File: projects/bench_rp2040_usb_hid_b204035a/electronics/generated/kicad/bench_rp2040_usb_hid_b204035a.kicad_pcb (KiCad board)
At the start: 2 copper layers, 51 x 21 mm, 14 parts, among them J1 USB-C POWER, J2 SWD 10-pin, U1 3V3 LDO, U2 RP2040, U3 2MB QSPI, X1 12MHz XTAL

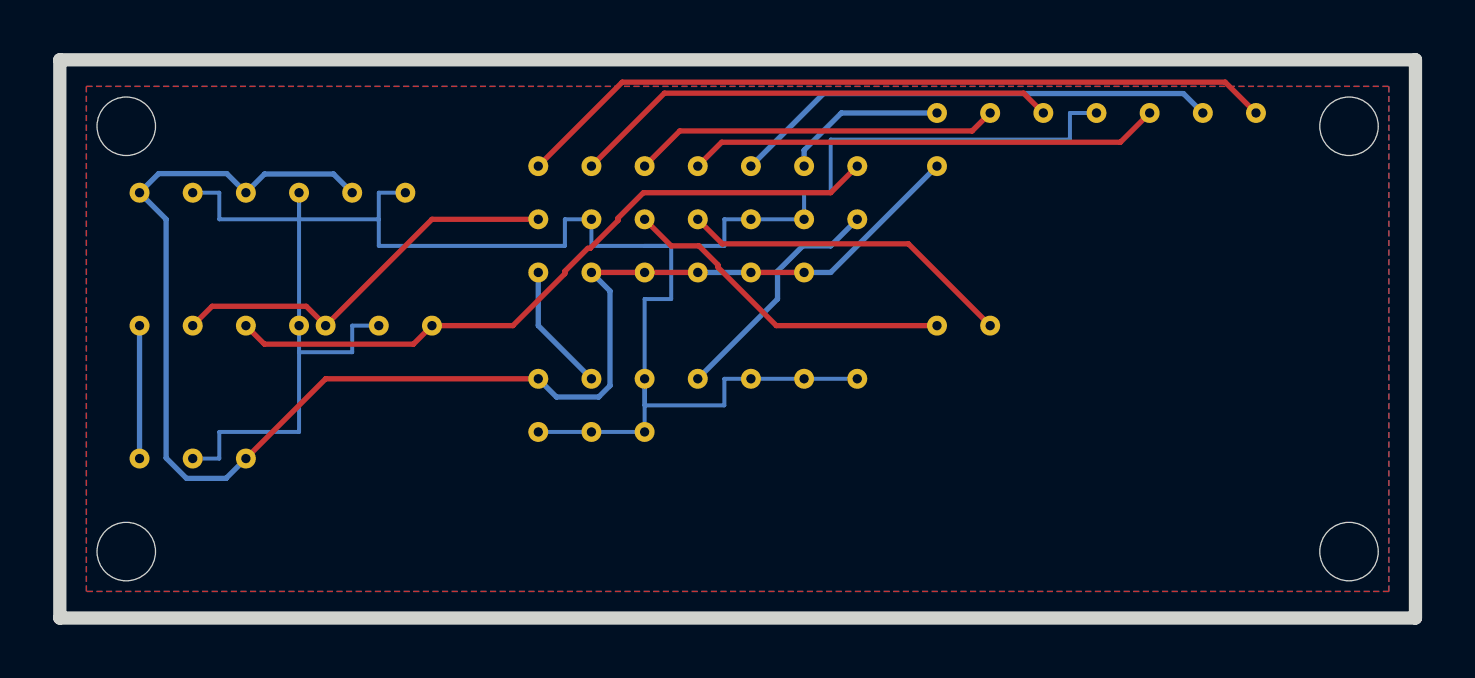
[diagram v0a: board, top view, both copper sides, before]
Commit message: fix: model rp2040 usb esd boundary
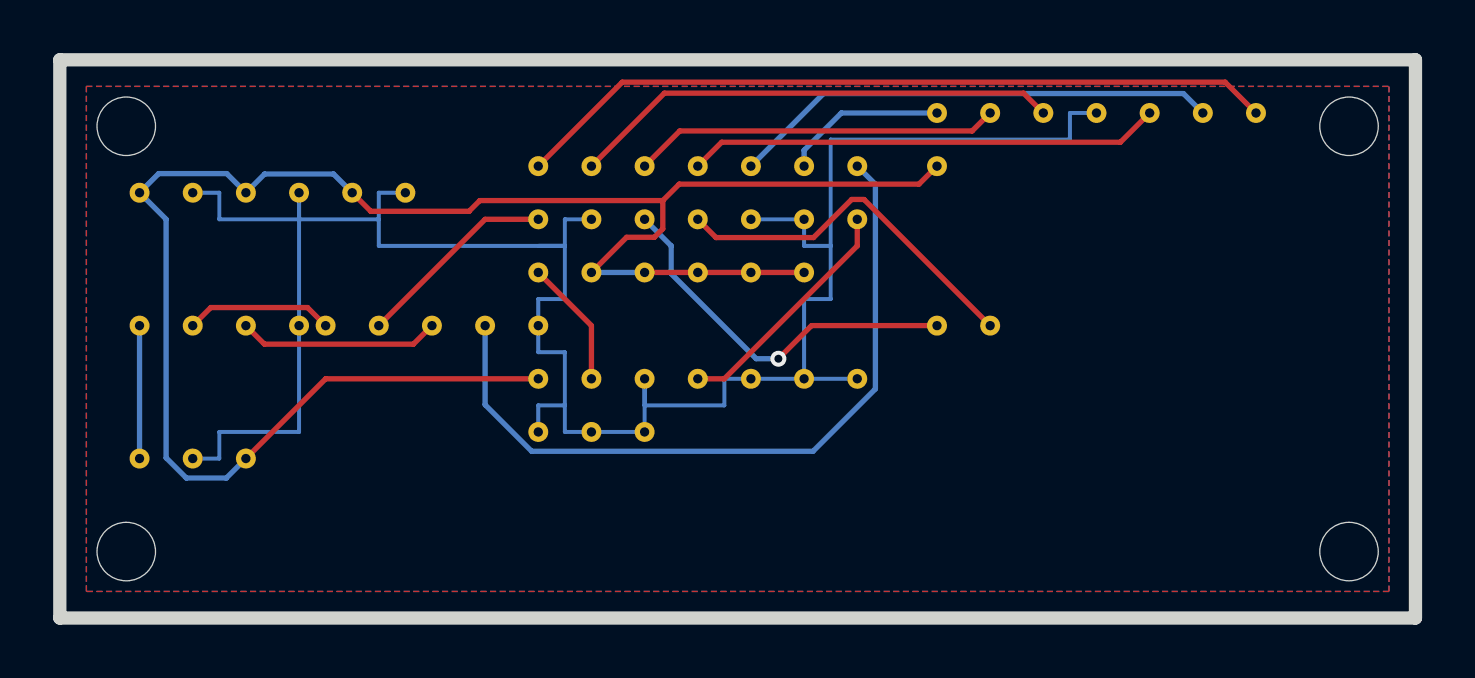
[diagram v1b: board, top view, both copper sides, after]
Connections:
- D1 pad 1: USB_DP -> USB_DP_RAW
- D1 pad 2: GND -> USB_DP
- D1 pad 3: USB_DM -> USB_DM_RAW
- J1 pad 2: USB_DP -> USB_DP_RAW
- J1 pad 3: USB_DM -> USB_DM_RAW
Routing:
- net V3V3: track 57.8 -> 70.8 mm
- net USB_DP: track 15.3 -> 7.66 mm
- net USB_DM_RAW: track 0.00 -> 7.58 mm
- net USB_DP_RAW: track 0.00 -> 5.56 mm
- net USB_DM: track 26.2 -> 28.0 mm
- net XIN: track 12.7 -> 14.3 mm, vias 0 -> 1
- net XOUT: track 12.7 -> 13.8 mm
